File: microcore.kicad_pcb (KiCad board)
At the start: 4 copper layers, 90 x 60 mm, 7 parts, among them J1 TE_776231-1, J8 USB_B_Mini, M1 Module:mega-mcu100/0.3, M2 Module-power_12and5V-0.3, M3 Module-vr-max9924-0.3

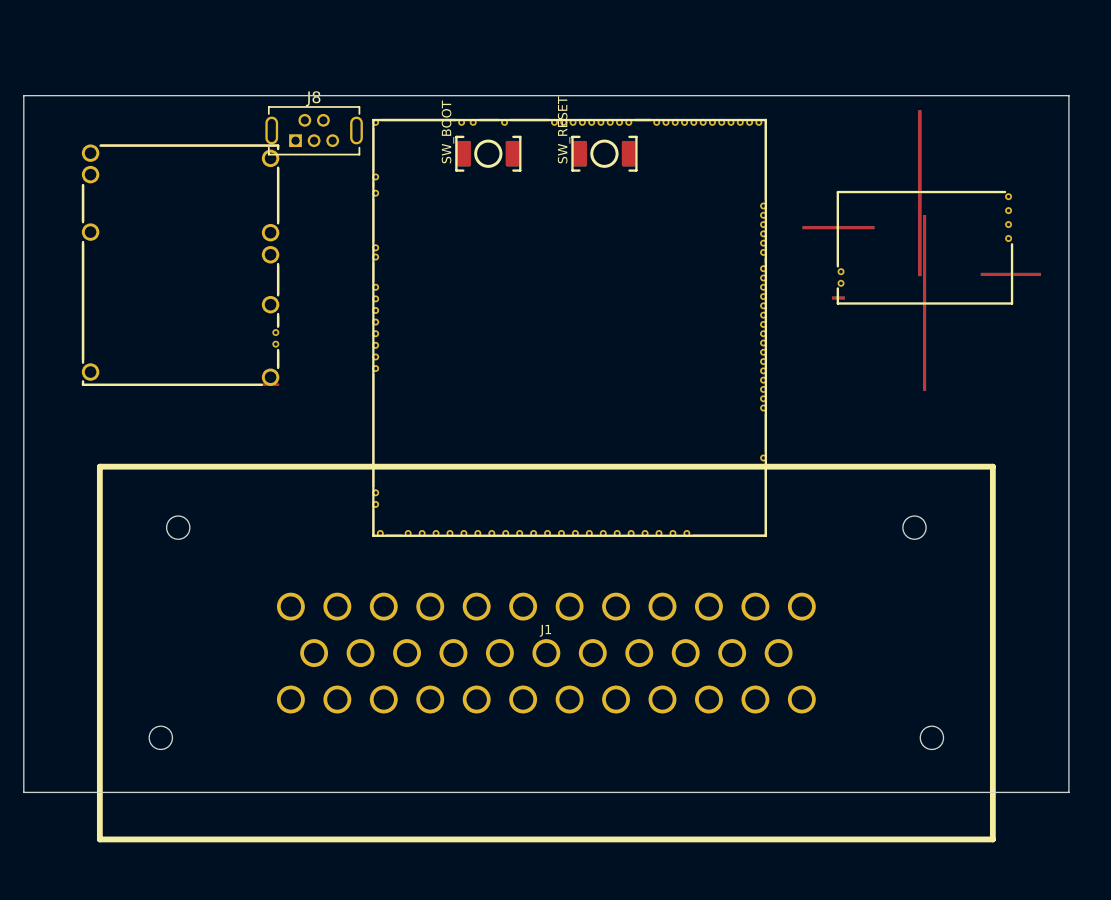
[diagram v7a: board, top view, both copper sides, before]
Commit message: Rev e: nest INJ/LS DPAKs on frame, apply netlist, GND pours, route
Place Q1-Q7 + R1-R7 clear of AMPSEAL keepout; unify GND global net;
assign schematic nets to pads; add F/B GND zones and scripted frame
tracks/vias. Module copper remains Create Board gerber merge.
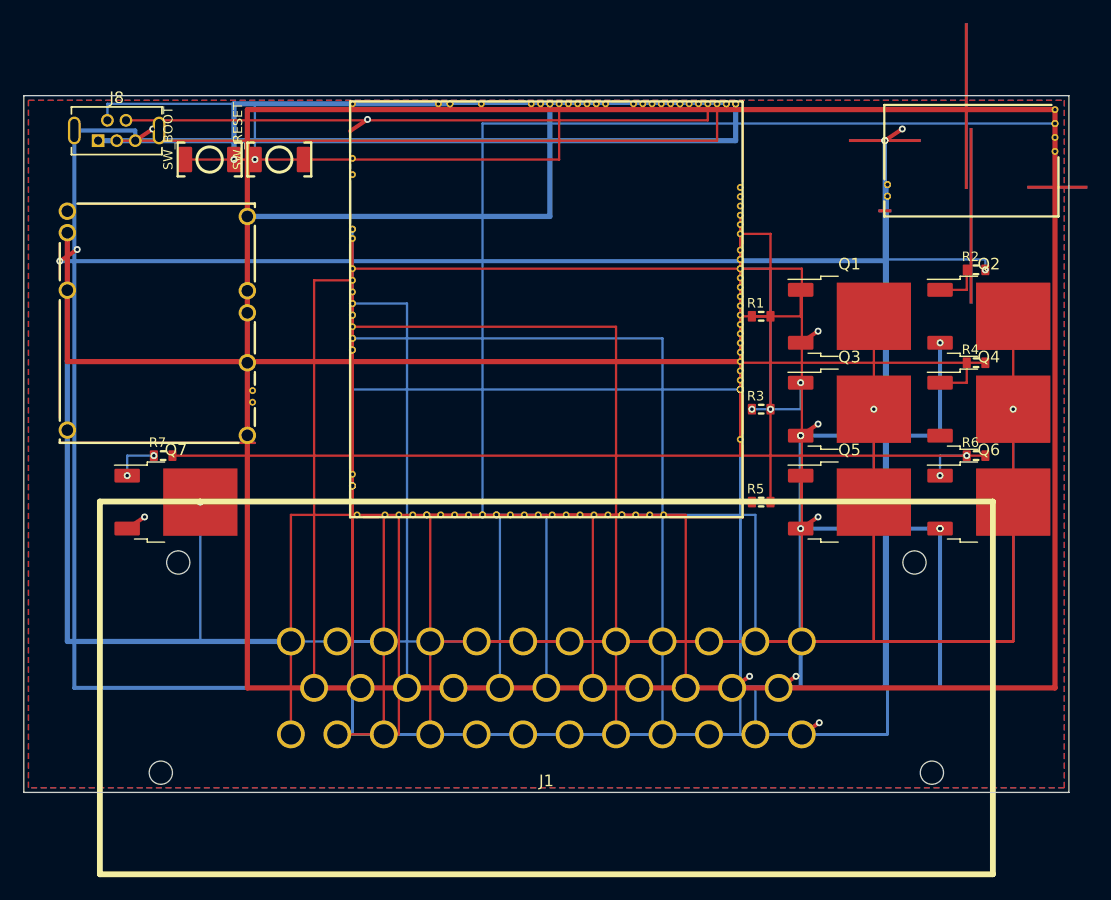
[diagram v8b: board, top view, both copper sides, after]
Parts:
- added Q1: VND14NV04-E, DPAK, F.Cu at (70.0, 19.0)
- added Q2: VND14NV04-E, DPAK, F.Cu at (82.0, 19.0)
- added Q3: VND14NV04-E, DPAK, F.Cu at (70.0, 27.0)
- added Q4: VND14NV04-E, DPAK, F.Cu at (82.0, 27.0)
- added Q5: VND14NV04-E, DPAK, F.Cu at (70.0, 35.0)
- added Q6: VND14NV04-E, DPAK, F.Cu at (82.0, 35.0)
- added Q7: VND14NV04-E, DPAK, F.Cu at (12.0, 35.0)
- added R1: 12, R0603, F.Cu at (63.5, 19.0)
- added R2: 12, R0603, F.Cu at (82.0, 15.0)
- added R3: 12, R0603, F.Cu at (63.5, 27.0)
- added R4: 12, R0603, F.Cu at (82.0, 23.0)
- added R5: 12, R0603, F.Cu at (63.5, 35.0)
- added R6: 12, R0603, F.Cu at (82.0, 31.0)
- added R7: 12, R0603, F.Cu at (12.0, 31.0)
- moved SW_RESET 28.0 mm to (22.0, 5.50)
- moved SW_BOOT 24.0 mm to (16.0, 5.50)
- moved J8 17.0 mm to (8.00, 3.00)
- moved M3 8.50 mm to (74.0, 10.5)
- moved M2 5.39 mm to (3.00, 30.0)
- moved J1 3.00 mm to (45.0, 51.0)
- moved M1 2.56 mm to (28.0, 36.4)
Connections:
- J1 pad 1: (no net) -> /V12_RAW
- J1 pad 10: (no net) -> /LS3_BOOST
- J1 pad 11: (no net) -> /DIN1
- J1 pad 12: (no net) -> /IGN1
- J1 pad 13: (no net) -> /IGN2
- J1 pad 14: (no net) -> /IGN3
- J1 pad 15: (no net) -> /IGN4
- J1 pad 16: (no net) -> /V5_REF
- J1 pad 17: (no net) -> /TPS
- J1 pad 18: (no net) -> /MAP
- J1 pad 19: (no net) -> /AN1
- J1 pad 2: (no net) -> /CAN_H
- J1 pad 20: (no net) -> /SGND
- J1 pad 21: (no net) -> /AN2
- J1 pad 22: (no net) -> GND
- J1 pad 23: (no net) -> GND
- J1 pad 24: (no net) -> /CLT
- J1 pad 25: (no net) -> /IAT
- J1 pad 26: (no net) -> /DIN2
- J1 pad 27: (no net) -> /HALL_CAM
- J1 pad 28: (no net) -> /VR_P
- J1 pad 29: (no net) -> /VR_N
- J1 pad 3: (no net) -> /CAN_L
- J1 pad 30: (no net) -> /IGN5
- J1 pad 31: (no net) -> /IGN6
- J1 pad 32: (no net) -> /IGN7
- J1 pad 33: (no net) -> /IGN8
- J1 pad 34: (no net) -> /SGND
- J1 pad 35: (no net) -> GND
- J1 pad 4: (no net) -> /INJ1
- J1 pad 5: (no net) -> /INJ2
- J1 pad 6: (no net) -> /INJ3
- J1 pad 7: (no net) -> /INJ4
- J1 pad 8: (no net) -> /LS1_FP
- J1 pad 9: (no net) -> /LS2_IDLE
- J8 pad 1: (no net) -> /VBUS
- J8 pad 2: (no net) -> /USBM_(PA11)
- J8 pad 3: (no net) -> /USBP_(PA12)
- J8 pad 4: (no net) -> /USBID_(PA10)
- J8 pad 5: (no net) -> GND
- J8 pad 6: (no net) -> GND
- M1 pad E14: (no net) -> /OUT_INJ4
- M1 pad E15: (no net) -> /OUT_INJ3
- M1 pad E16: (no net) -> /OUT_INJ2
- M1 pad E17: (no net) -> /OUT_INJ1
- M1 pad E18: (no net) -> /OUT_LS1
- M1 pad E19: (no net) -> /OUT_LS2
- M1 pad E2: (no net) -> /SGND
- M1 pad E20: (no net) -> /OUT_LS3
- M1 pad E5: (no net) -> /VIGN_SENSE
- M1 pad G: (no net) -> GND
- M1 pad N1: (no net) -> /VBUS
- M1 pad N16: (no net) -> /BOOT0
- M1 pad N17: (no net) -> /VBAT
- M1 pad N2: (no net) -> /USBM_(PA11)
- M1 pad N21: (no net) -> /V33
- M1 pad N3: (no net) -> /USBP_(PA12)
- M1 pad N4: (no net) -> /USBID_(PA10)
- M1 pad N7: (no net) -> /nReset
- M1 pad S13: (no net) -> /MAP
- M1 pad S14: (no net) -> /VR_OUT
- M1 pad S16: (no net) -> /HALL_CAM
- M1 pad S18: (no net) -> /TPS
- M1 pad S20: (no net) -> /IAT
- M1 pad S21: (no net) -> /CLT
- M1 pad S3: (no net) -> /DIN2
- M1 pad S4: (no net) -> /DIN1
- M1 pad S8: (no net) -> /AN2
- M1 pad S9: (no net) -> /AN1
- M1 pad W1: (no net) -> /SGND
- M1 pad W10: (no net) -> /IGN1
- M1 pad W11: (no net) -> /CAN_H
- M1 pad W12: (no net) -> /CAN_L
- M1 pad W3: (no net) -> /IGN8
- M1 pad W4: (no net) -> /IGN7
- M1 pad W5: (no net) -> /IGN6
- M1 pad W6: (no net) -> /IGN5
- M1 pad W7: (no net) -> /IGN4
- M1 pad W8: (no net) -> /IGN3
- M1 pad W9: (no net) -> /IGN2
- M2 pad E1: (no net) -> /VBAT
- M2 pad E3: (no net) -> /VIGN
- M2 pad E4: (no net) -> /V5_REF
- M2 pad S1: (no net) -> GND
- M2 pad V2: (no net) -> /VIGN_SENSE
- M2 pad V3: (no net) -> /V12_RAW
- M3 pad E3: (no net) -> /VR_OUT
- M3 pad E4: (no net) -> /V5_REF
- M3 pad G: (no net) -> GND
- M3 pad W1: (no net) -> /VR_N
- M3 pad W2: (no net) -> /VR_P
- SW_BOOT pad 1: (no net) -> /BOOT0
- SW_BOOT pad 2: (no net) -> /V33
- SW_RESET pad 1: (no net) -> /nReset
- SW_RESET pad 2: (no net) -> GND
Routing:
- net GND: track 0.00 -> 367.6 mm, vias 0 -> 29
- net /V5_REF: track 0.00 -> 238.7 mm
- net /SGND: track 0.00 -> 163.2 mm, vias 0 -> 10
- net /VR_OUT: track 0.00 -> 83.0 mm, vias 0 -> 2
- net /VR_P: track 0.00 -> 81.7 mm, vias 0 -> 2
- net /VR_N: track 0.00 -> 78.7 mm, vias 0 -> 2
- net /INJ2: track 0.00 -> 74.2 mm
- net /IGN1: track 0.00 -> 70.8 mm
- net /OUT_LS3: track 0.00 -> 69.6 mm
- net /VIGN_SENSE: track 0.00 -> 69.1 mm
- net /INJ1: track 0.00 -> 66.2 mm
- net /IGN8: track 0.00 -> 63.8 mm, vias 0 -> 2
- net /IGN7: track 0.00 -> 60.8 mm, vias 0 -> 2
- net /INJ4: track 0.00 -> 58.2 mm, vias 0 -> 2
- net /VBUS: track 0.00 -> 58.1 mm, vias 0 -> 2
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- added copper zone on B.Cu, net GND
- added copper zone on F.Cu, net GND
